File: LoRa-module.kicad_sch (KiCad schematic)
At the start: 24 parts, among them J1 5035661102, M1 0900FM15K0039001E, U1 SX1262IMLTRT, U2 IPEX-1

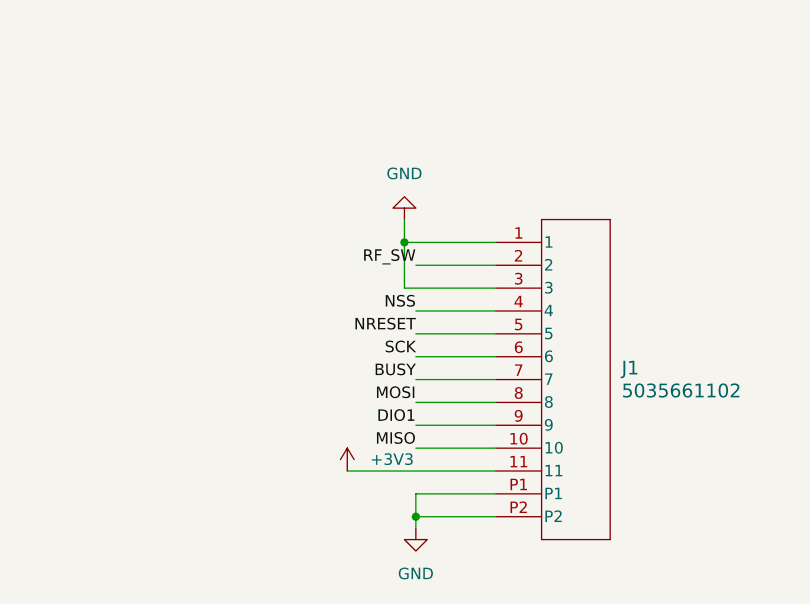
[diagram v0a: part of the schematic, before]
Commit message: Updated FPC pinout
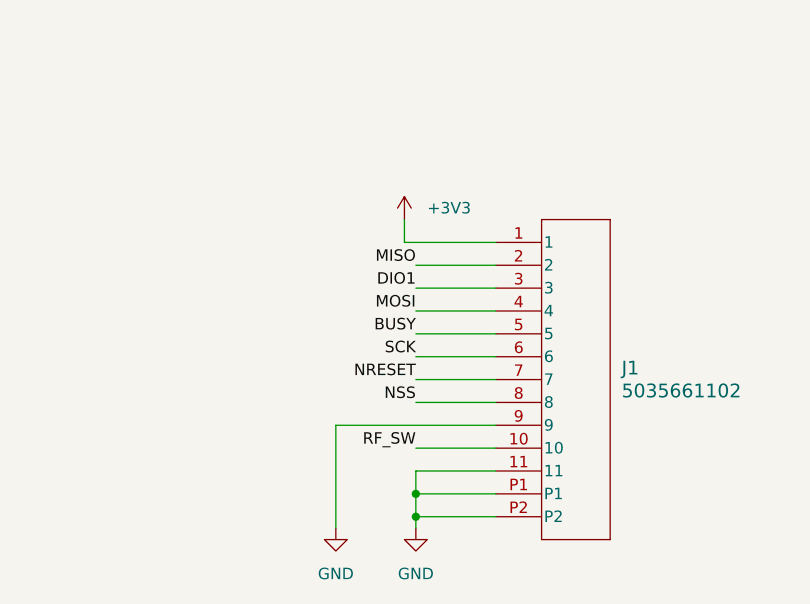
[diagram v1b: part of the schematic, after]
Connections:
- net +3V3: now also J1.1; no longer J1.11
- net BUSY: now also J1.5; no longer J1.7
- net DIO1: now also J1.3; no longer J1.9
- net GND: now also J1.11, J1.9; no longer J1.1, J1.3
- net MISO: now also J1.2; no longer J1.10
- net MOSI: now also J1.4; no longer J1.8
- net NRESET: now also J1.7; no longer J1.5
- net NSS: now also J1.8; no longer J1.4
- net RF_SW: now also J1.10; no longer J1.2
